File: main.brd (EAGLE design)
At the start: 121.3 x 51.7 mm, 29 parts, among them IC1 MEGA88, IC2 AMS1117-5.0, Q1 32768Hz, Q2 BC817, Q3 IRF7473, SW1 EC12E_SW

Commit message: добавил дополнительную землю от Moffet
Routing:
- net GND: track 348.2 -> 368.5 mm, vias 0 -> 2
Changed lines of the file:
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@@
 <wire x1="53.34" y1="10.795" x2="53.34" y2="7.62" width="0.4" layer="1"/>
 <wire x1="53.34" y1="7.62" x2="53.975" y2="6.985" width="0.4" layer="1"/>
-<wire x1="12.7" y1="5.08" x2="30.48" y2="5.08" width="0.8" layer="1"/>
+<wire x1="12.7" y1="5.08" x2="24.13" y2="5.08" width="0.8" layer="1"/>
+<wire x1="24.13" y1="5.08" x2="30.48" y2="5.08" width="0.8" layer="1"/>
 <wire x1="53.975" y1="6.985" x2="59.055" y2="6.985" width="0.4" layer="1"/>
 <wire x1="59.055" y1="6.985" x2="63.5" y2="6.985" width="0.4" layer="1"/>
@@
 <contactref element="R15" pad="1"/>
 <wire x1="39.37" y1="9.525" x2="43.815" y2="9.525" width="0.4064" layer="1"/>
+<wire x1="24.13" y1="25.4" x2="24.13" y2="5.08" width="0.8" layer="16"/>
+<wire x1="22.225" y1="8.89" x2="24.13" y2="5.08" width="0" layer="19" extent="1-16"/>
+<via x="24.13" y="25.4" extent="1-16" drill="0.6" shape="square"/>
+<via x="24.13" y="5.08" extent="1-16" drill="0.6" shape="square"/>
 </signal>
 <signal name="+5V">

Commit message: Заменил AMS1117 на LM7805. От 12В AMS1117 сглючивает и сжигает атмегу
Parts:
- removed IC2: AMS1117-5.0, v-reg:SOT223
- added IC3: 7805TV, linear:TO220V
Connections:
- net +12V: now also IC3.1; no longer IC2.3
- net +5V: now also IC3.3; no longer IC2.4
- net GND: now also IC3.2; no longer IC2.1
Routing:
- net +12V: track 39.2 -> 41.2 mm
- net +5V: track 211.7 -> 213.4 mm
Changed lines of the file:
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@@
 <attribute name="MF" value="" x="57.15" y="27.305" size="1.778" layer="27" rot="R270" display="off"/>
 </element>
-<element name="IC2" library="v-reg" package="SOT223" value="AMS1117-5.0" x="30.1625" y="23.1775" rot="R270"/>
 <element name="JP2" library="pinhead" package="1X02" value="" x="4.445" y="25.0825" rot="R90"/>
 <element name="LCD1" library="lcd_2x16_led_backlight" package="HY-1602F" value="LCD_2X16_SIL" x="27.94" y="15.24" rot="MR180"/>
@@
 <element name="R14" library="rcl" package="R1206" value="0" x="40.64" y="23.495" rot="R90"/>
 <element name="R15" library="rcl" package="RTRIM3296W" value="" x="36.83" y="9.525" rot="MR270"/>
+<element name="IC3" library="linear" package="TO220V" value="7805TV" x="29.21" y="20.32" rot="MR180"/>
 </elements>
 <signals>
@@
 <signal name="+12V">
 <contactref element="JP2" pad="1"/>
-<contactref element="IC2" pad="3"/>
 <contactref element="C2" pad="1"/>
 <contactref element="X2" pad="2"/>
@@
 <wire x1="17.78" y1="20.955" x2="20.32" y2="20.955" width="0.8" layer="1"/>
 <wire x1="20.32" y1="20.955" x2="21.59" y2="19.685" width="0.8" layer="1"/>
-<wire x1="21.59" y1="19.685" x2="25.5025" y2="19.685" width="0.8" layer="1"/>
-<wire x1="25.5025" y1="19.685" x2="27.0125" y2="20.8775" width="0.8" layer="1"/>
+<wire x1="21.59" y1="19.685" x2="26.035" y2="19.685" width="0.8" layer="1"/>
 <wire x1="4.445" y1="23.8125" x2="9.525" y2="23.8125" width="0.8" layer="1"/>
 <wire x1="9.525" y1="23.8125" x2="10.4775" y2="23.8125" width="0.8" layer="1"/>
@@
 <wire x1="15.9512" y1="10.2362" x2="17.78" y2="12.065" width="0.8" layer="1"/>
 <wire x1="17.78" y1="12.065" x2="17.78" y2="20.955" width="0.8" layer="1"/>
+<contactref element="IC3" pad="1"/>
+<wire x1="26.035" y1="19.685" x2="26.67" y2="20.32" width="0.8" layer="1"/>
+<wire x1="26.67" y1="20.32" x2="26.67" y2="22.86" width="0.8" layer="1"/>
 </signal>
 <signal name="GND" airwireshidden="yes">
@@
 <contactref element="Q2" pad="E"/>
 <contactref element="C1" pad="2"/>
-<contactref element="IC2" pad="1"/>
 <contactref element="C2" pad="2"/>
 <contactref element="C3" pad="2"/>
@@
 <wire x1="30.48" y1="5.08" x2="30.48" y2="15.24" width="0.8" layer="1"/>
 <wire x1="21.015" y1="25.4" x2="24.13" y2="25.4" width="0.8" layer="1"/>
-<wire x1="24.13" y1="25.4" x2="26.935" y2="25.4" width="0.8" layer="1"/>
-<wire x1="26.935" y1="25.4" x2="27.0125" y2="25.4775" width="0.8" layer="1"/>
+<wire x1="24.13" y1="25.4" x2="26.67" y2="25.4" width="0.8" layer="1"/>
+<wire x1="26.67" y1="25.4" x2="26.935" y2="25.4" width="0.8" layer="1"/>
 <wire x1="21.015" y1="24.13" x2="23.495" y2="24.13" width="0.8" layer="1"/>
 <wire x1="23.495" y1="24.13" x2="24.13" y2="24.765" width="0.8" layer="1"/>
@@
 <wire x1="9.525" y1="8.255" x2="9.525" y2="10.1981" width="0.8" layer="1"/>
 <wire x1="9.525" y1="10.1981" x2="9.5631" y2="10.2362" width="0.8" layer="1"/>
-<wire x1="29.21" y1="27.94" x2="29.21" y2="25.4" width="0.8" layer="1"/>
-<wire x1="29.21" y1="25.4" x2="29.21" y2="19.05" width="0.8" layer="1"/>
-<wire x1="29.21" y1="19.05" x2="29.21" y2="16.51" width="0.8" layer="1"/>
 <wire x1="29.21" y1="16.51" x2="30.48" y2="15.24" width="0.8" layer="1"/>
 <wire x1="29.21" y1="27.94" x2="29.5275" y2="28.2575" width="0.8" layer="1"/>
-<wire x1="27.0125" y1="25.4775" x2="29.1325" y2="25.4775" width="0.8" layer="1"/>
-<wire x1="29.1325" y1="25.4775" x2="29.21" y2="25.4" width="0.8" layer="1"/>
 <wire x1="29.5275" y1="28.2575" x2="30.5675" y2="28.2575" width="0.8" layer="1"/>
 <wire x1="37.465" y1="19.3675" x2="29.5275" y2="19.3675" width="0.4" layer="1"/>
@@
 <wire x1="39.37" y1="9.525" x2="43.815" y2="9.525" width="0.4064" layer="1"/>
 <wire x1="24.13" y1="25.4" x2="24.13" y2="5.08" width="0.8" layer="16"/>
-<wire x1="22.225" y1="8.89" x2="24.13" y2="5.08" width="0" layer="19" extent="1-16"/>
 <via x="24.13" y="25.4" extent="1-16" drill="0.6" shape="square"/>
 <via x="24.13" y="5.08" extent="1-16" drill="0.6" shape="square"/>
+<contactref element="IC3" pad="2"/>
+<wire x1="29.21" y1="16.51" x2="29.21" y2="25.4" width="0.8" layer="1"/>
+<wire x1="29.21" y1="25.4" x2="29.21" y2="27.94" width="0.8" layer="1"/>
+<wire x1="26.935" y1="25.4" x2="29.21" y2="25.4" width="0.8" layer="1"/>
+<wire x1="29.21" y1="25.4" x2="29.21" y2="22.86" width="0" layer="19" extent="1-1"/>
 </signal>
 <signal name="+5V">
@@
 <contactref element="R5" pad="2"/>
 <contactref element="R4" pad="2"/>
-<contactref element="IC2" pad="4"/>
 <contactref element="C3" pad="1"/>
 <wire x1="56.75" y1="21.5075" x2="56.515" y2="21.2725" width="0.4" layer="1"/>
@@
 <wire x1="52.705" y1="21.2725" x2="50.4825" y2="23.495" width="0.4" layer="1"/>
 <wire x1="55.15" y1="21.3675" x2="55.245" y2="21.2725" width="0.4" layer="1"/>
-<wire x1="33.63" y1="23.495" x2="33.3125" y2="23.1775" width="0.4" layer="1"/>
+<contactref element="R1" pad="2"/>
 <wire x1="33.63" y1="23.495" x2="34.925" y2="23.495" width="0.4" layer="1"/>
-<contactref element="R1" pad="2"/>
 <wire x1="34.925" y1="23.495" x2="43.18" y2="23.495" width="0.4" layer="1"/>
 <wire x1="43.18" y1="23.495" x2="48.26" y2="23.495" width="0.4" layer="1"/>
@@
 <wire x1="33.02" y1="9.677" x2="34.29" y2="9.677" width="0.4064" layer="1"/>
 <wire x1="34.29" y1="9.677" x2="34.29" y2="9.525" width="0.4064" layer="1"/>
+<contactref element="IC3" pad="3"/>
+<wire x1="31.75" y1="22.86" x2="32.995" y2="22.86" width="0.6" layer="1"/>
+<wire x1="32.995" y1="22.86" x2="33.63" y2="23.495" width="0.6" layer="1"/>
 <wire x1="33.02" y1="9.677" x2="33.02" y2="9.525" width="0" layer="19" extent="1-1"/>
 </signal>

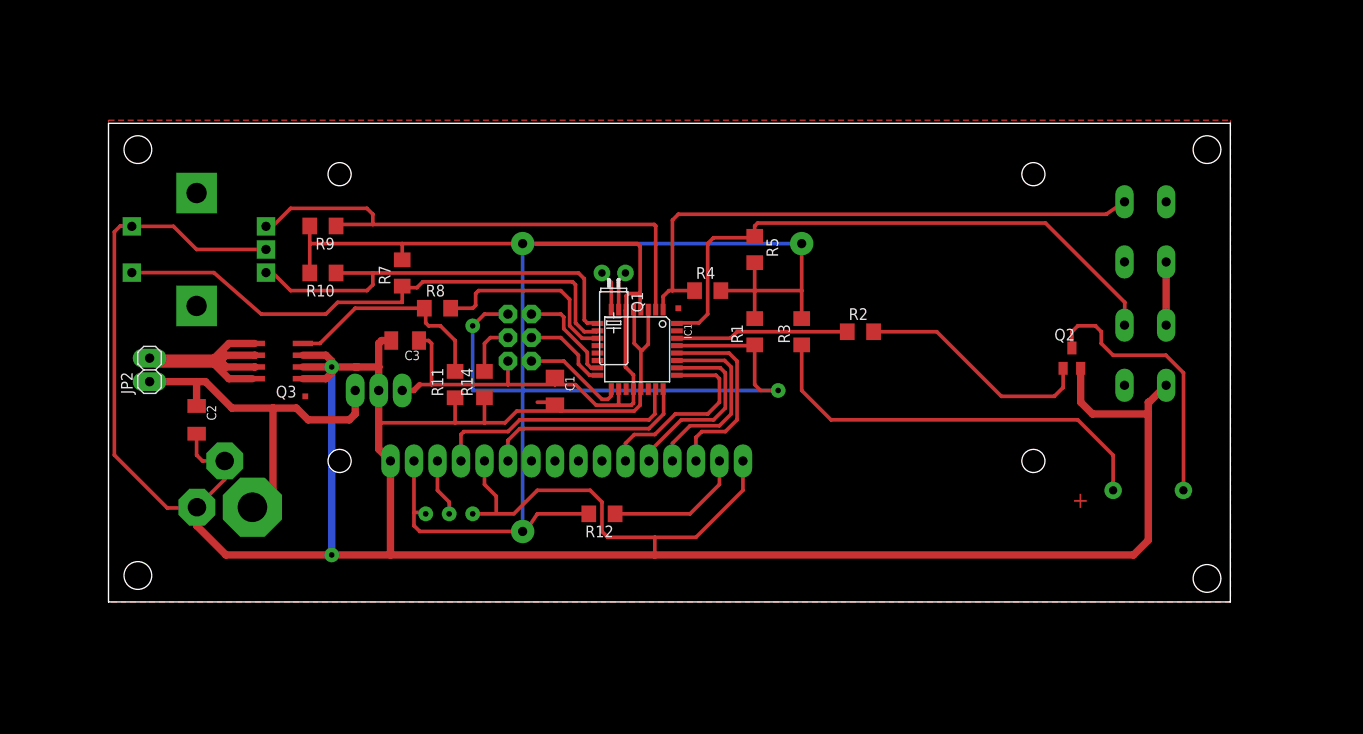
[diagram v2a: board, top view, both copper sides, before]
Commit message: Чуть пеерделал схему. Добавил файл для печати в типографии с маской и шелкографией
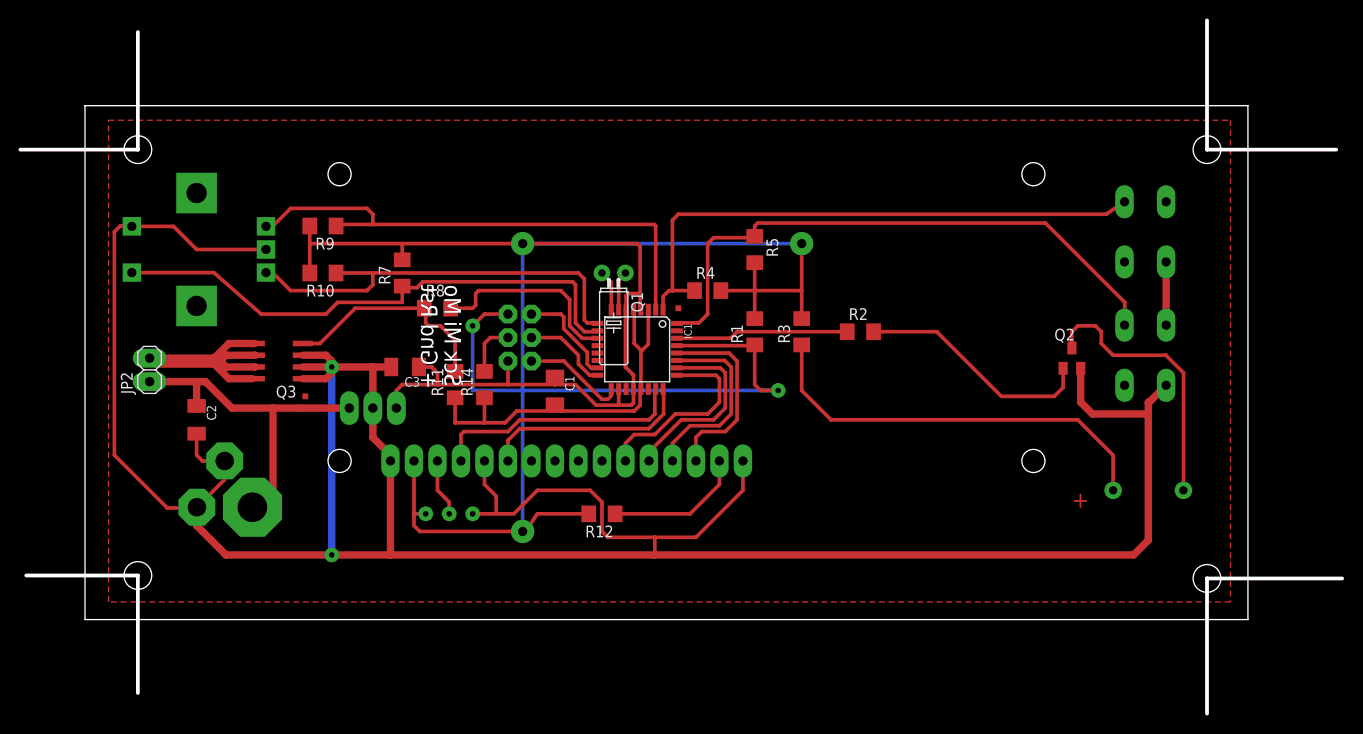
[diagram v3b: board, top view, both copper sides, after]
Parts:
- moved C3 2.86 mm to (32.1, 25.4)
- moved IC3 2.01 mm to (28.6, 18.4)
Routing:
- net GND: track 368.4 -> 357.6 mm
- net +12V: track 41.2 -> 37.3 mm
- net N$7: track 1.27 -> 0.00 mm
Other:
- board size 121.3 x 51.7 mm -> 142.9 x 74.9 mm
- board text added: "+ Gnd Rst"
- board text added: "Sck Mi Mo"

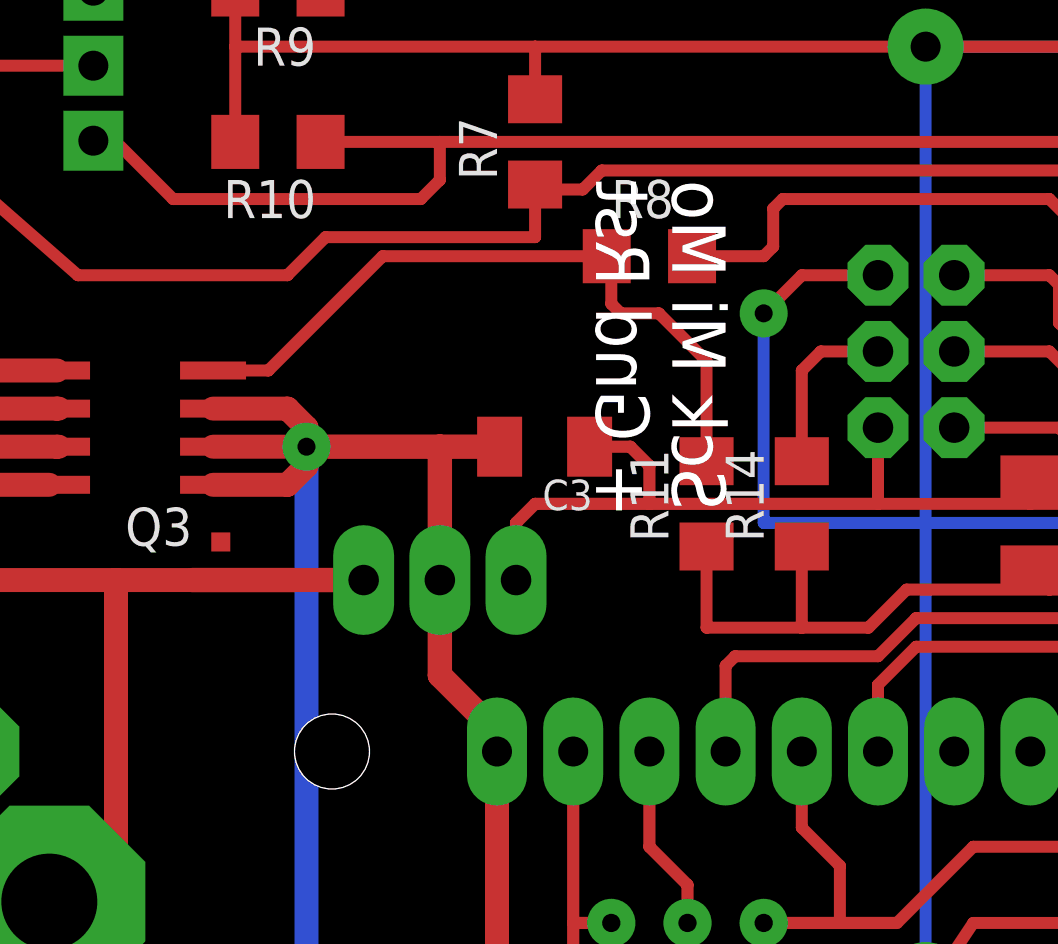
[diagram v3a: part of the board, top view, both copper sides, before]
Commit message: Исправил ошибку на печатке, не была соединена земля LM7805 и земля Atmega о_О (орел жжет) Исправил печатку маски (правильно выводить tStop)
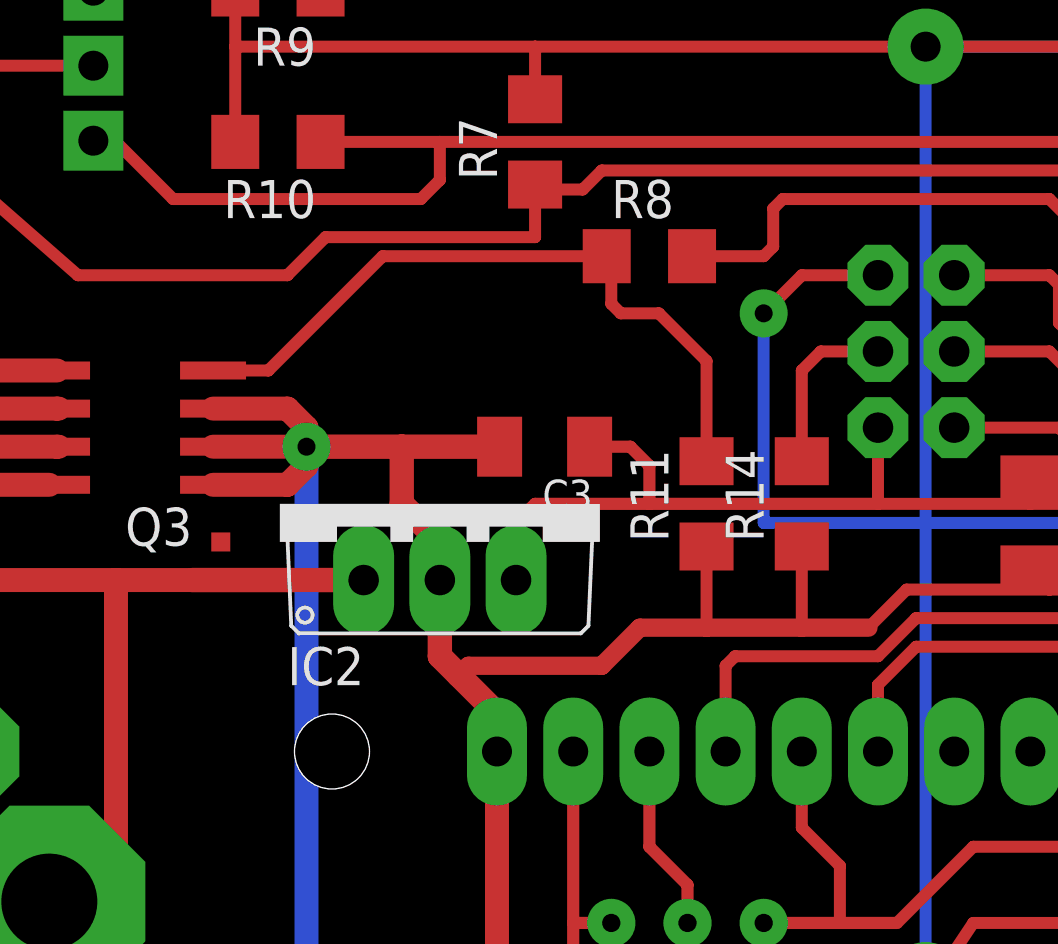
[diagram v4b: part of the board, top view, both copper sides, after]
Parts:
- removed IC3: 7805TV, linear:TO220V
- added IC2: 7805TV, linear:TO220V
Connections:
- net +12V: now also IC2.1; no longer IC3.1
- net +5V: now also IC2.3; no longer IC3.3
- net GND: now also IC2.2; no longer IC3.2
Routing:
- net GND: track 357.6 -> 367.0 mm
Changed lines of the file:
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@@
 <wire x1="133.35" y1="2.54" x2="118.745" y2="2.54" width="0.4064" layer="20"/>
 <wire x1="3.175" y1="2.8575" x2="-8.89" y2="2.8575" width="0.4064" layer="20"/>
-<text x="38.1" y="34.29" size="1.778" layer="20" rot="MR270">Sck Mi Mo</text>
-<text x="35.56" y="34.29" size="1.778" layer="20" rot="MR270">+ Gnd Rst</text>
+<text x="37.465" y="34.29" size="1.778" layer="26" rot="MR270">Sck Mi Mo</text>
+<text x="35.56" y="34.29" size="1.778" layer="26" rot="MR270">+ Gnd Rst</text>
 </plain>
 <attributes>
@@
 <element name="R14" library="rcl" package="R1206" value="0" x="40.64" y="23.495" rot="R90"/>
 <element name="R15" library="rcl" package="RTRIM3296W" value="" x="36.83" y="9.525" rot="MR270"/>
-<element name="IC3" library="linear" package="TO220V" value="7805TV" x="28.575" y="18.415" rot="MR180"/>
+<element name="IC2" library="linear" package="TO220V" value="7805TV" x="28.575" y="23.495"/>
 </elements>
 <signals>
@@
 <wire x1="15.9512" y1="10.2362" x2="17.78" y2="12.065" width="0.8" layer="1"/>
 <wire x1="17.78" y1="12.065" x2="17.78" y2="20.955" width="0.8" layer="1"/>
-<contactref element="IC3" pad="1"/>
-<wire x1="20.32" y1="20.955" x2="26.035" y2="20.955" width="0.8128" layer="1"/>
+<contactref element="IC2" pad="1"/>
+<wire x1="26.035" y1="20.955" x2="20.32" y2="20.955" width="0.8128" layer="1"/>
 </signal>
 <signal name="GND" airwireshidden="yes">
@@
 <wire x1="58.35" y1="31.5976" x2="58.35" y2="27.87" width="0.4" layer="1"/>
 <wire x1="44.1325" y1="20.6375" x2="42.8625" y2="19.3675" width="0.4" layer="1"/>
-<wire x1="42.8625" y1="19.3675" x2="40.64" y2="19.3675" width="0.4" layer="1"/>
-<wire x1="40.64" y1="19.3675" x2="37.465" y2="19.3675" width="0.4" layer="1"/>
+<wire x1="42.8625" y1="19.3675" x2="40.64" y2="19.3675" width="0.6096" layer="1"/>
+<wire x1="40.64" y1="19.3675" x2="37.465" y2="19.3675" width="0.6096" layer="1"/>
 <wire x1="37.465" y1="22.073" x2="37.465" y2="19.3675" width="0.4" layer="1"/>
 <wire x1="40.64" y1="15.24" x2="40.64" y2="12.7" width="0.4" layer="1"/>
@@
 <via x="24.13" y="25.4" extent="1-16" drill="0.6" shape="square"/>
 <via x="24.13" y="5.08" extent="1-16" drill="0.6" shape="square"/>
-<contactref element="IC3" pad="2"/>
-<wire x1="30.48" y1="25.4" x2="28.575" y2="25.4" width="0.8128" layer="1"/>
-<wire x1="28.575" y1="25.4" x2="24.13" y2="25.4" width="0.8128" layer="1"/>
-<wire x1="30.48" y1="15.24" x2="30.48" y2="15.875" width="0.8128" layer="1"/>
-<wire x1="30.48" y1="15.875" x2="28.575" y2="17.78" width="0.8128" layer="1"/>
-<wire x1="28.575" y1="17.78" x2="28.575" y2="20.955" width="0.8128" layer="1"/>
-<wire x1="28.575" y1="20.955" x2="28.575" y2="25.4" width="0.8128" layer="1"/>
-<wire x1="40.64" y1="19.3675" x2="40.64" y2="15.24" width="0" layer="19" extent="1-1"/>
+<wire x1="30.48" y1="25.4" x2="27.305" y2="25.4" width="0.8128" layer="1"/>
+<wire x1="27.305" y1="25.4" x2="24.13" y2="25.4" width="0.8128" layer="1"/>
+<contactref element="IC2" pad="2"/>
+<wire x1="27.305" y1="25.4" x2="27.305" y2="23.495" width="0.8128" layer="1"/>
+<wire x1="27.305" y1="23.495" x2="28.575" y2="22.225" width="0.8128" layer="1"/>
+<wire x1="28.575" y1="22.225" x2="28.575" y2="18.415" width="0.8128" layer="1"/>
+<wire x1="28.575" y1="18.415" x2="29.21" y2="17.78" width="0.8128" layer="1"/>
+<wire x1="29.21" y1="17.78" x2="30.48" y2="16.51" width="0.8128" layer="1"/>
+<wire x1="30.48" y1="16.51" x2="30.48" y2="15.24" width="0.8128" layer="1"/>
+<wire x1="37.465" y1="19.3675" x2="35.2425" y2="19.3675" width="0.6096" layer="1"/>
+<wire x1="35.2425" y1="19.3675" x2="33.9725" y2="18.0975" width="0.6096" layer="1"/>
+<wire x1="33.9725" y1="18.0975" x2="29.5275" y2="18.0975" width="0.6096" layer="1"/>
+<wire x1="29.5275" y1="18.0975" x2="29.21" y2="17.78" width="0.6096" layer="1"/>
+<wire x1="28.575" y1="22.225" x2="28.575" y2="20.955" width="0" layer="19" extent="1-1"/>
 </signal>
 <signal name="+5V">
@@
 <wire x1="74.93" y1="33.655" x2="74.93" y2="30.632" width="0.4" layer="1"/>
 <contactref element="R15" pad="3"/>
-<contactref element="IC3" pad="3"/>
 <wire x1="43.18" y1="23.495" x2="35.56" y2="23.495" width="0.4064" layer="1"/>
 <wire x1="35.56" y1="23.495" x2="31.75" y2="23.495" width="0.4064" layer="1"/>
-<wire x1="31.115" y1="20.955" x2="31.115" y2="22.86" width="0.4064" layer="1"/>
 <wire x1="31.115" y1="22.86" x2="31.75" y2="23.495" width="0.4064" layer="1"/>
 <wire x1="33.5675" y1="25.4" x2="34.925" y2="25.4" width="0.4064" layer="1"/>
@@
 <wire x1="33.02" y1="9.525" x2="33.02" y2="15.24" width="0.4064" layer="1"/>
 <wire x1="34.29" y1="9.525" x2="33.02" y2="9.525" width="0.4064" layer="1"/>
+<contactref element="IC2" pad="3"/>
+<wire x1="31.115" y1="20.955" x2="31.115" y2="22.86" width="0.4064" layer="1"/>
 </signal>
 <signal name="N$1">
